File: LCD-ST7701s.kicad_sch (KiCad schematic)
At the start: 8 parts, among them J2 Conn_01x40_MountingPin, U3 TPS61042DRBT

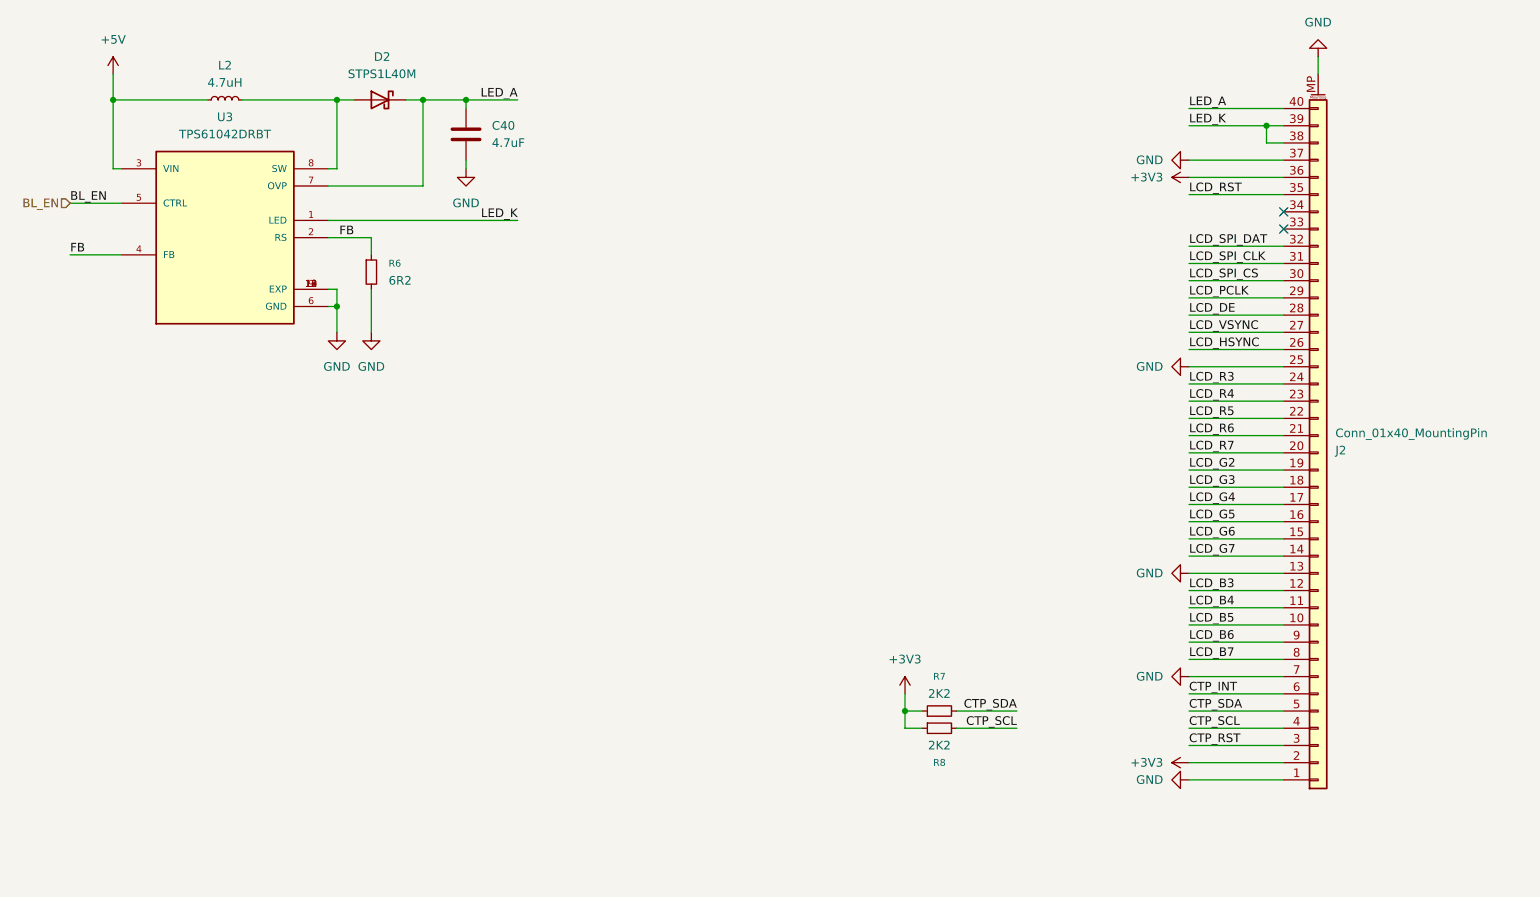
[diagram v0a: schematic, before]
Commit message: Added Battery Fuel Gauge, Battery Charger and 5V boost voltage
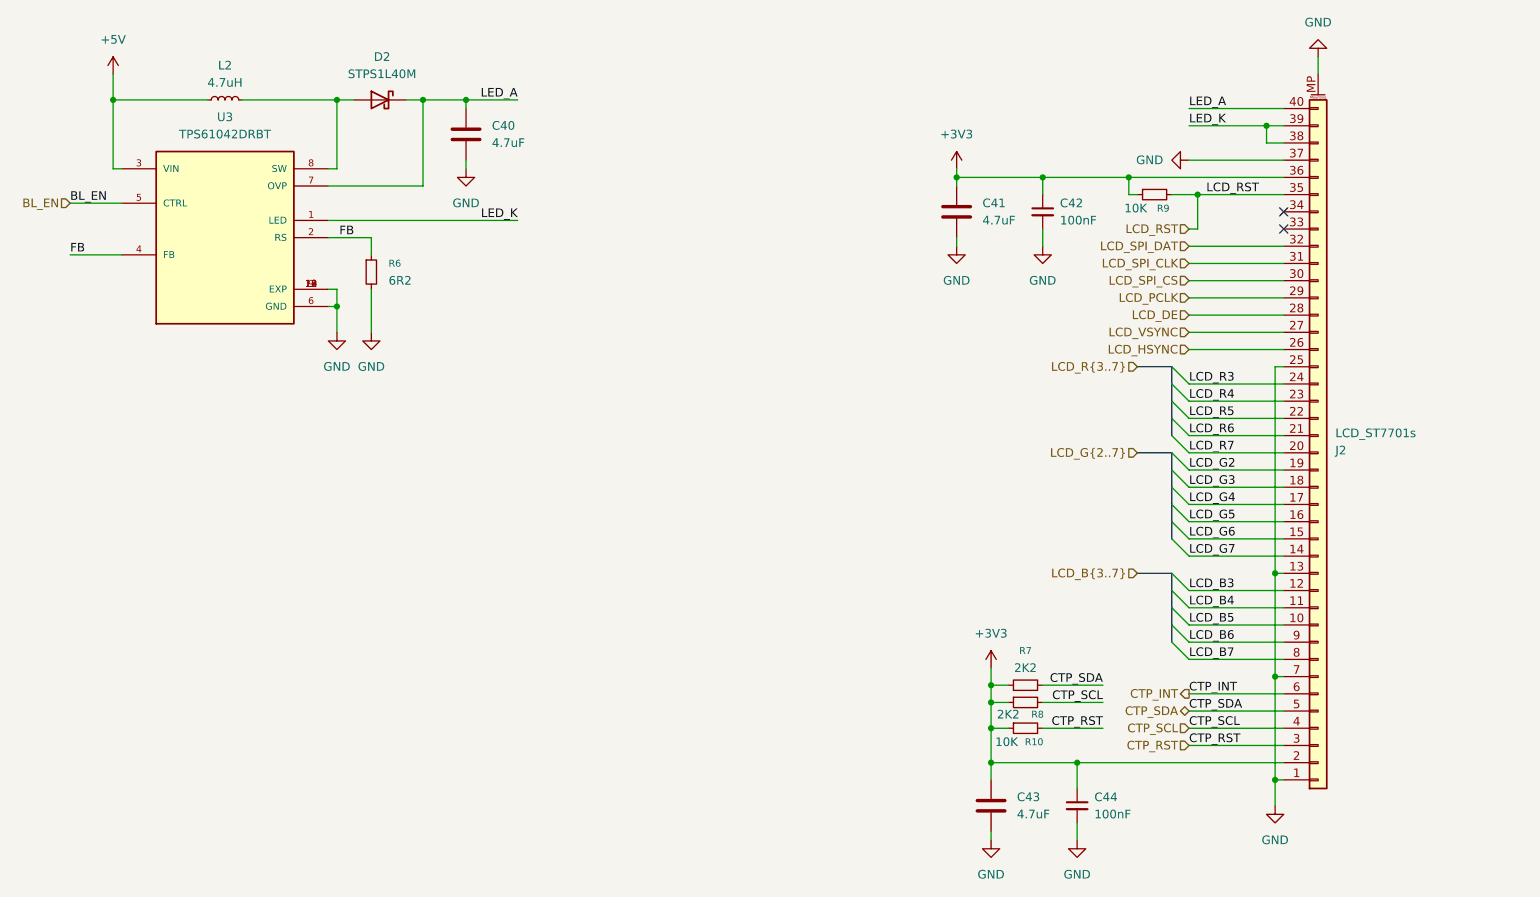
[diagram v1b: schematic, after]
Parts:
- added C41, C43: 4.7uF, symbol Device:C
- added C42, C44: 100nF, symbol Device:C_Small
- added R10, R9: 10K, symbol Device:R_Small
- J2: value Conn_01x40_MountingPin -> LCD_ST7701s
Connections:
- net +3V3: now also C41.1, C42.1, C43.1, C44.1, R10.1, R9.1
- net CTP_RST: now also R10.2
- net GND: now also C41.2, C42.2, C43.2, C44.2
- net LCD_RST: now also R9.2
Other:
- moved on the sheet: R7, R8

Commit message: layouting component to PCB
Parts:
- C40, C41, C43: footprint (none) -> Capacitor_SMD:C_0603_1608Metric
- C42, C44: footprint (none) -> Capacitor_SMD:C_0402_1005Metric
- D2: footprint (none) -> Diode_SMD:D_SMA
- J2: footprint (none) -> Connector_FFC-FPC:Omron_XF2M-4015-1A_1x40-1MP_P0.5mm_Horizontal
- L2: footprint (none) -> Inductor_SMD:L_Abracon_ASPI-0425
- R10, R6, R7, R8, R9: footprint (none) -> Resistor_SMD:R_0402_1005Metric
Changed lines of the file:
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@@
 			)
 		)
-		(property "Footprint" ""
+		(property "Footprint" "Resistor_SMD:R_0402_1005Metric"
 			(at 189.23 127 0)
 			(effects
@@
 			)
 		)
-		(property "Footprint" ""
+		(property "Footprint" "Connector_FFC-FPC:Omron_XF2M-4015-1A_1x40-1MP_P0.5mm_Horizontal"
 			(at 232.41 86.36 0)
 			(effects
@@
 			)
 		)
-		(property "Footprint" ""
+		(property "Footprint" "Inductor_SMD:L_Abracon_ASPI-0425"
 			(at 71.12 34.29 0)
 			(effects
@@
 			)
 		)
-		(property "Footprint" ""
+		(property "Footprint" "Resistor_SMD:R_0402_1005Metric"
 			(at 189.23 123.19 0)
 			(effects
@@
 			)
 		)
-		(property "Footprint" ""
+		(property "Footprint" "Diode_SMD:D_SMA"
 			(at 93.98 34.29 0)
 			(effects
@@
 			)
 		)
-		(property "Footprint" ""
+		(property "Footprint" "Resistor_SMD:R_0402_1005Metric"
 			(at 92.71 59.69 0)
 			(effects
@@
 			)
 		)
-		(property "Footprint" ""
+		(property "Footprint" "Capacitor_SMD:C_0603_1608Metric"
 			(at 107.6452 43.18 0)
 			(effects
@@
 			)
 		)
-		(property "Footprint" ""
+		(property "Footprint" "Capacitor_SMD:C_0603_1608Metric"
 			(at 185.1152 142.24 0)
 			(effects
@@
 			)
 		)
-		(property "Footprint" ""
+		(property "Footprint" "Capacitor_SMD:C_0603_1608Metric"
 			(at 180.0352 54.61 0)
 			(effects
@@
 			)
 		)
-		(property "Footprint" ""
+		(property "Footprint" "Resistor_SMD:R_0402_1005Metric"
 			(at 208.28 48.26 0)
 			(effects
@@
 			)
 		)
-		(property "Footprint" ""
+		(property "Footprint" "Capacitor_SMD:C_0402_1005Metric"
 			(at 196.85 138.43 0)
 			(effects
@@
 			)
 		)
-		(property "Footprint" ""
+		(property "Footprint" "Capacitor_SMD:C_0402_1005Metric"
 			(at 191.77 50.8 0)
 			(effects
@@
 			)
 		)
-		(property "Footprint" ""
+		(property "Footprint" "Resistor_SMD:R_0402_1005Metric"
 			(at 189.23 120.65 0)
 			(effects

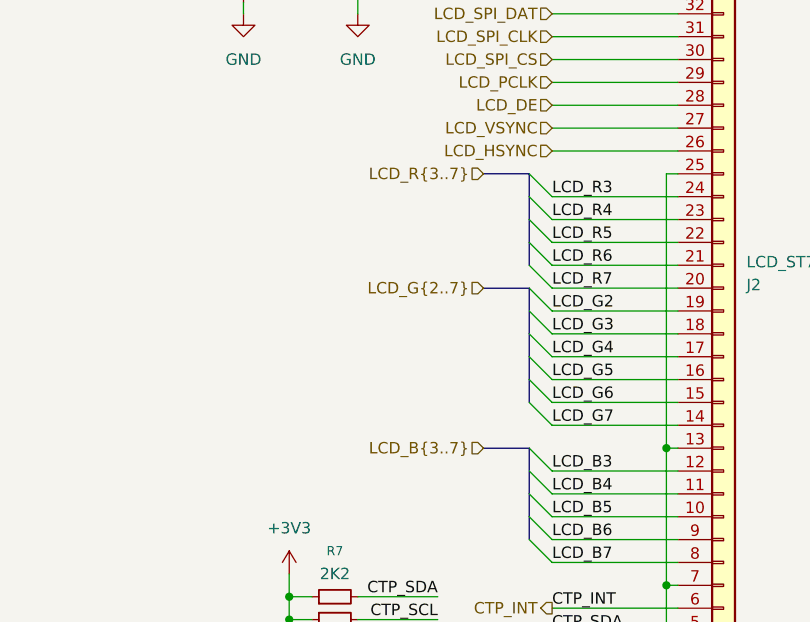
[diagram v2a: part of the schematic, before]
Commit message: Add connection from OSPI Flash and LCD to MCU
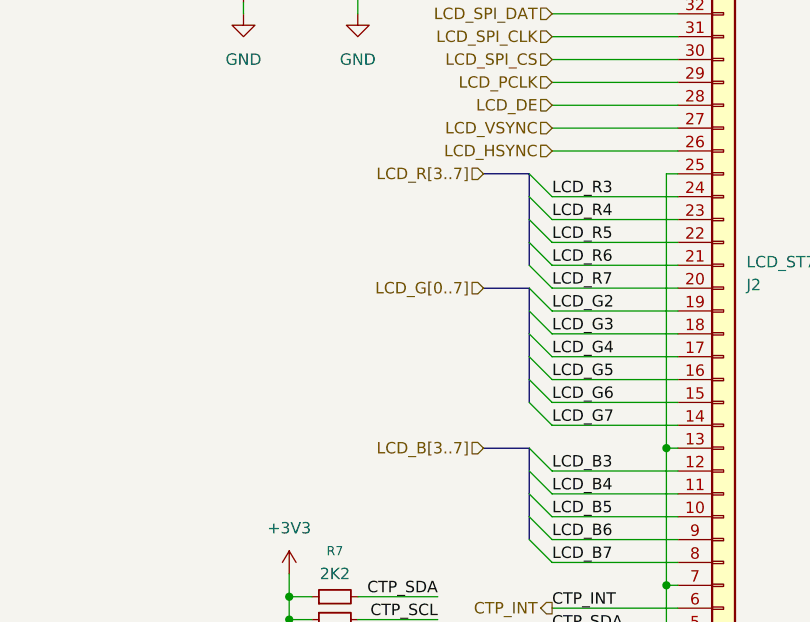
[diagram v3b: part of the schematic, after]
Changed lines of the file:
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@@
 		)
 	)
-	(hierarchical_label "LCD_B{3..7}"
+	(hierarchical_label "LCD_B[3..7]"
 		(shape input)
 		(at 205.74 104.14 180)
@@
 		)
 	)
-	(hierarchical_label "LCD_G{2..7}"
+	(hierarchical_label "LCD_G[0..7]"
 		(shape input)
 		(at 205.74 86.36 180)
@@
 		)
 	)
-	(hierarchical_label "LCD_R{3..7}"
+	(hierarchical_label "LCD_R[3..7]"
 		(shape input)
 		(at 205.74 73.66 180)

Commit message: Change bypass capacitor to 0201
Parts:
- C42, C44: footprint Capacitor_SMD:C_0402_1005Metric -> Capacitor_SMD:C_0201_0603Metric
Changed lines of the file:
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@@
 			)
 		)
-		(property "Footprint" "Capacitor_SMD:C_0402_1005Metric"
+		(property "Footprint" "Capacitor_SMD:C_0201_0603Metric"
 			(at 196.85 138.43 0)
 			(effects
@@
 			)
 		)
-		(property "Footprint" "Capacitor_SMD:C_0402_1005Metric"
+		(property "Footprint" "Capacitor_SMD:C_0201_0603Metric"
 			(at 191.77 50.8 0)
 			(effects
